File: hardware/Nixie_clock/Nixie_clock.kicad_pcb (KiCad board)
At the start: 2 copper layers, 204 x 60.8 mm, 77 parts, among them J1 90814-0912, J10 Conn_01x02_Pin, J11 12V_IN, J12 UART, J13 Conn_01x02_Pin, J14 Debug1, J16 Debug, J2 90814-0912, J3 90814-0912, J4 90814-0912, J5 90814-0912, J6 90814-0912, J7 90814-0912, J8 90814-0912, J9 Conn_01x02_Pin, Q1 PMV37ENEAR, Q2 PMV37ENEAR, Q3 PMV37ENEAR, Q4 PMV37ENEAR, Q5 PMV37ENEAR, SW1 SW_Toggle_DPDT, U1 MAX1771xSA, U2 ESP32-C3-MINI-1, U3 TLV76133DCY, Y1 coil

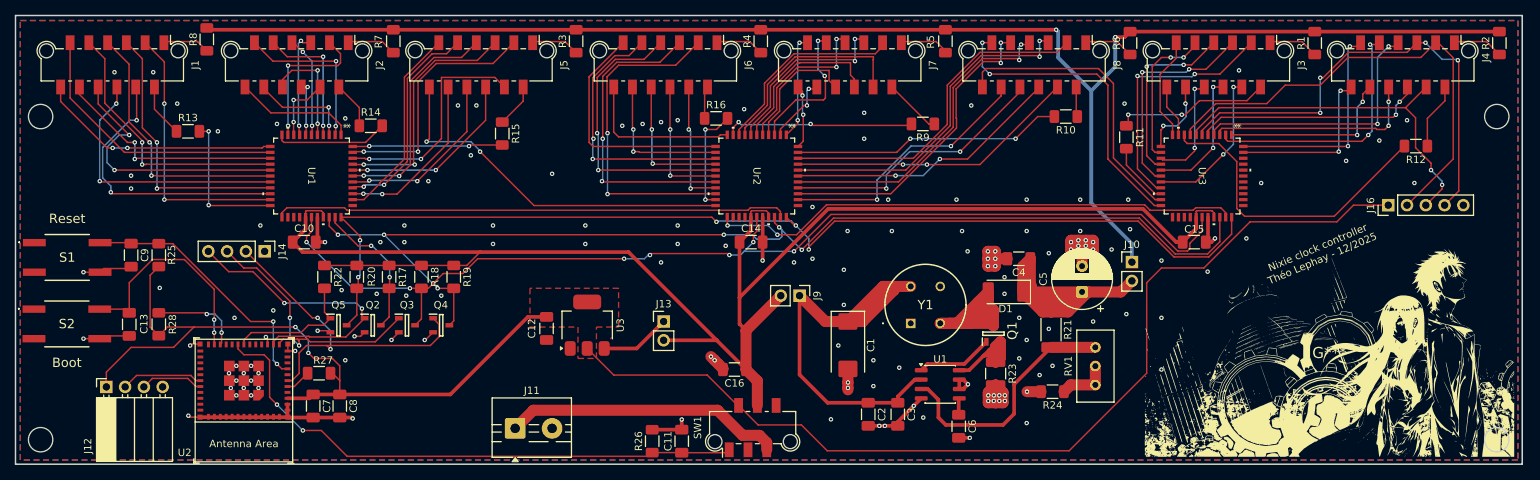
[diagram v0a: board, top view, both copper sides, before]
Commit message: Hardware revision 1.1
Fix: HV5622 pad spacing, use bigger DCDC FET, add LS NFETs PD resistors, Minor layout fixes.
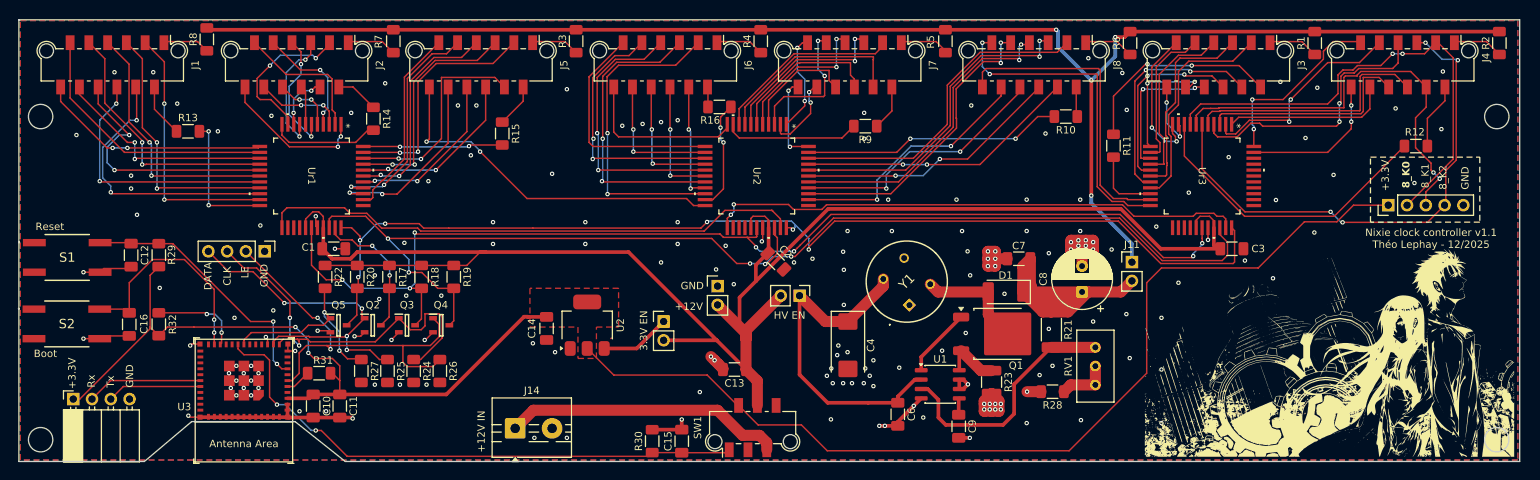
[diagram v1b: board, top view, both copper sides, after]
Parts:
- removed the C2 at (165.8, 129.8)
- added J16: Conn_01x02_Pin, Connector_PinHeader_2.54mm:PinHeader_1x02_P2.54mm_Vertical, F.Cu at (145.4, 112.5)
- added R24: 10k, Resistor_SMD:R_1206_3216Metric_Pad1.30x1.75mm_HandSolder, F.Cu at (104.3, 124.0)
- added R25: 10k, Resistor_SMD:R_1206_3216Metric_Pad1.30x1.75mm_HandSolder, F.Cu at (100.7, 124.0)
- added R26: 10k, Resistor_SMD:R_1206_3216Metric_Pad1.30x1.75mm_HandSolder, F.Cu at (107.8, 124.0)
- added R27: 3.6k, Resistor_SMD:R_1206_3216Metric_Pad1.30x1.75mm_HandSolder, F.Cu at (97.2, 124.0)
- J10: renamed from J9; value Conn_01x02_Pin -> HV_EN
- J13: value Conn_01x02_Pin -> 3.3V_EN
- Q1: value PMV37ENEAR -> IPD60R280P7; footprint PMV37ENEAR:SOT95P230X110-3N -> Package_TO_SOT_SMD:TO-252-2
- R17, R18, R19, R20: value 10k -> 4.7k
- SW1: value SW_Toggle_DPDT -> Tog_ON_ON_(ON)
- Y1: value coil -> AIUR-08 coil
- moved R9 7.81 mm to (165.4, 90.8)
- moved C3 5.18 mm to (215.0, 107.4)
- moved J15 4.77 mm to (58.2, 127.8)
- moved C2 4.24 mm to (153.3, 109.1), turned to -45 degrees
- moved C1 4.10 mm to (93.4, 107.4)
- moved Y1 2.48 mm to (171.4, 115.0), turned to 45 degrees
- moved R11 2.09 mm to (199.0, 93.5)
- moved R16 1.61 mm to (145.7, 88.2)
- moved R23 1.27 mm to (182.5, 125.5)
- moved R14 1.01 mm to (98.8, 89.8), turned to -90 degrees
- moved Q1 0.67 mm to (183.4, 118.9), turned to 0 degrees
- moved R22 0.08 mm to (92.3, 111.2)
- moved R20 0.06 mm to (96.6, 111.2)
- renumbered C10 to C1, C7 to C10, C8 to C11, C9 to C12, C16 to C13, C12 to C14, C11 to C15, C13 to C16, C14 to C2, C15 to C3, C1 to C4, C3 to C6, C4 to C7, C5 to C8, C6 to C9, J10 to J11, J14 to J12, J11 to J14, J12 to J15, J16 to J9, R24 to R28, R25 to R29, R26 to R30, R27 to R31, R28 to R32, U3 to U2, U2 to U3
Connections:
- net /LS1_in renamed /LS_data_in
- net /LS1_out renamed /LS_data_out
- net /LS2_in renamed /LS_clk_in
- net /LS2_out renamed /LS_clk_out
- net /LS3_in renamed /LS_LE_in
- net /LS3_out renamed /LS_LE_out
- net /LS4_in renamed /LS_BL_in
- net /LS4_out renamed /LS_BL_out
- Q1 pad 2: Net-(U1-CS) -> Net-(D1-A)
- Q1 pad 3: Net-(D1-A) -> Net-(Q1-S)
- R23 pad 1: Net-(U1-CS) -> Net-(Q1-S)
- U1 pad 8: Net-(U1-CS) -> Net-(Q1-S)
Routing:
- net /LS_clk_in: track 36.8 -> 53.3 mm
- net Net-(D1-A): track 30.3 -> 15.0 mm
- net Net-(U1-CS): track 15.0 -> 0.00 mm
- net GND: track 122.1 -> 108.8 mm, vias 151 -> 181
- net Net-(J10-Pin_1): track 57.5 -> 46.3 mm
- net /Nixie_7_K1: track 20.8 -> 31.2 mm
- net /LS_BL_in: track 17.9 -> 27.4 mm, vias 0 -> 2
- net Net-(Q1-S): track 0.00 -> 7.98 mm
- net /LS_data_in: track 39.6 -> 47.5 mm, vias 2 -> 4
- net /LS_LE_in: track 46.6 -> 54.5 mm
- net /Nixie_7_K3: track 17.9 -> 25.7 mm
- net Net-(Ur2-HVOUT13): track 25.8 -> 18.4 mm, vias 2 -> 0
- net /Nixie_2_K5: track 15.0 -> 8.29 mm
- net /Nixie_8_K1: track 50.3 -> 56.9 mm
- net Net-(J3-C): track 21.7 -> 28.2 mm
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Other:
- board size 204 x 60.8 mm -> 203.2 x 59.8 mm
- board text added: "+12V"
- board text added: "+12V IN"
- board text added: "+3.3V"
- board text added: "3.3V EN"
- board text added: "8_K0"
- board text added: "8_K1"
- board text added: "8_K2"
- board text added: "CLK"
- board text added: "DATA"
- board text added: "GND"
- board text added: "HV EN"
- board text added: "LE"
- board text added: "Nixie clock controller v1.1 Théo Lephay - 12/2025"
- board text added: "Rx"
- board text added: "Tx"
- board text removed: "Nixie clock controller Théo Lephay - 12/2025"
